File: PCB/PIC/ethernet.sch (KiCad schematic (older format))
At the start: 49 parts, among them J5 RJ45-TRANSFO, U1 LAN_8740, U2 SI502

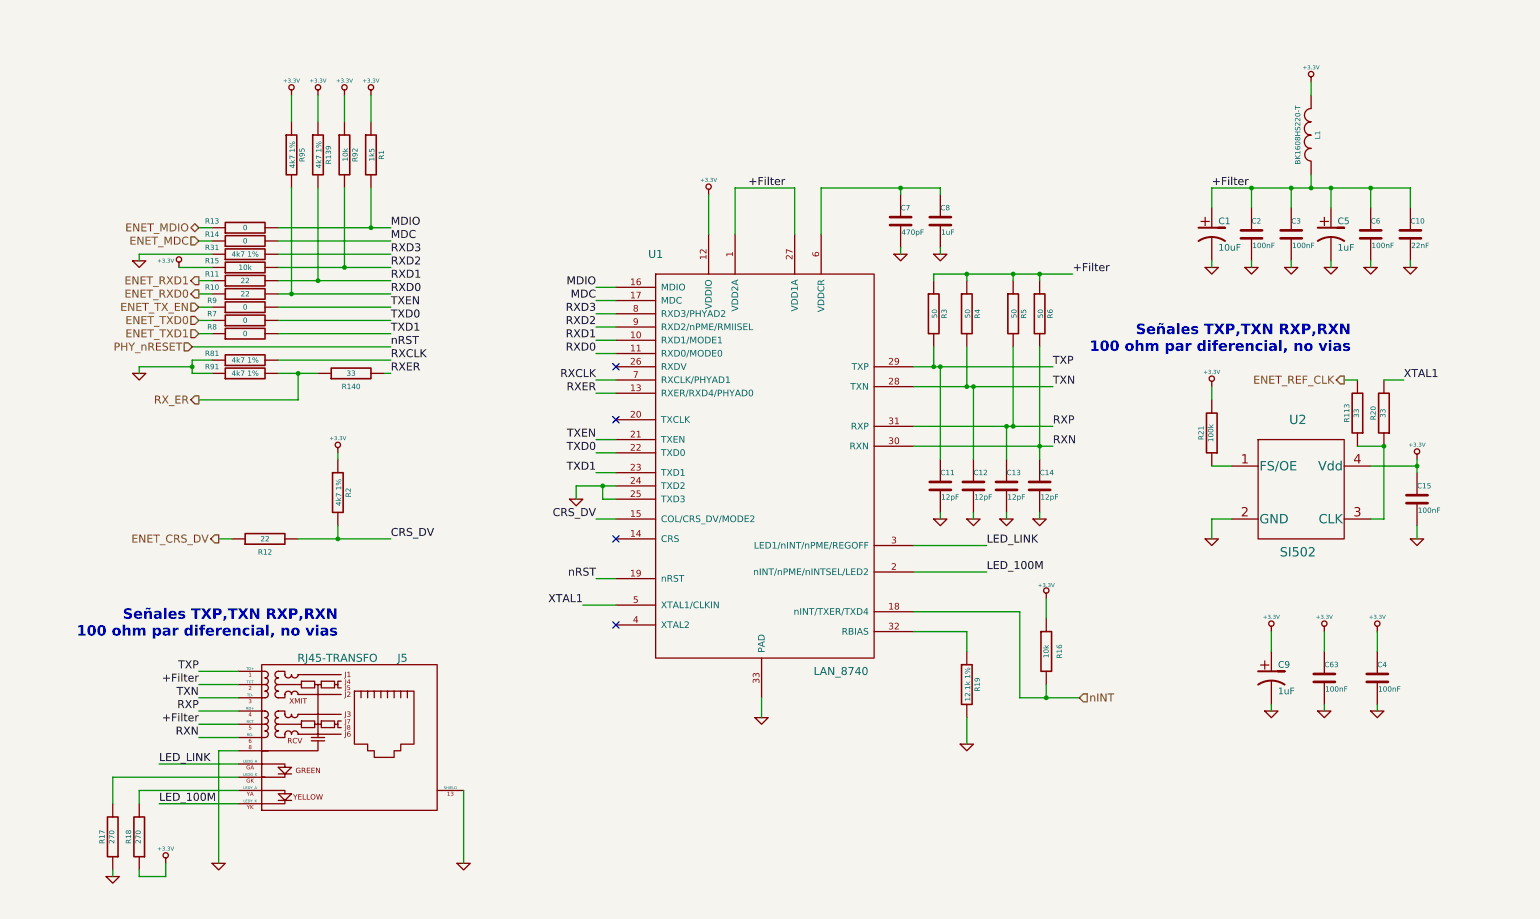
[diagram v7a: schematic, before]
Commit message: se completan pisadas componentes CIAA-PIC
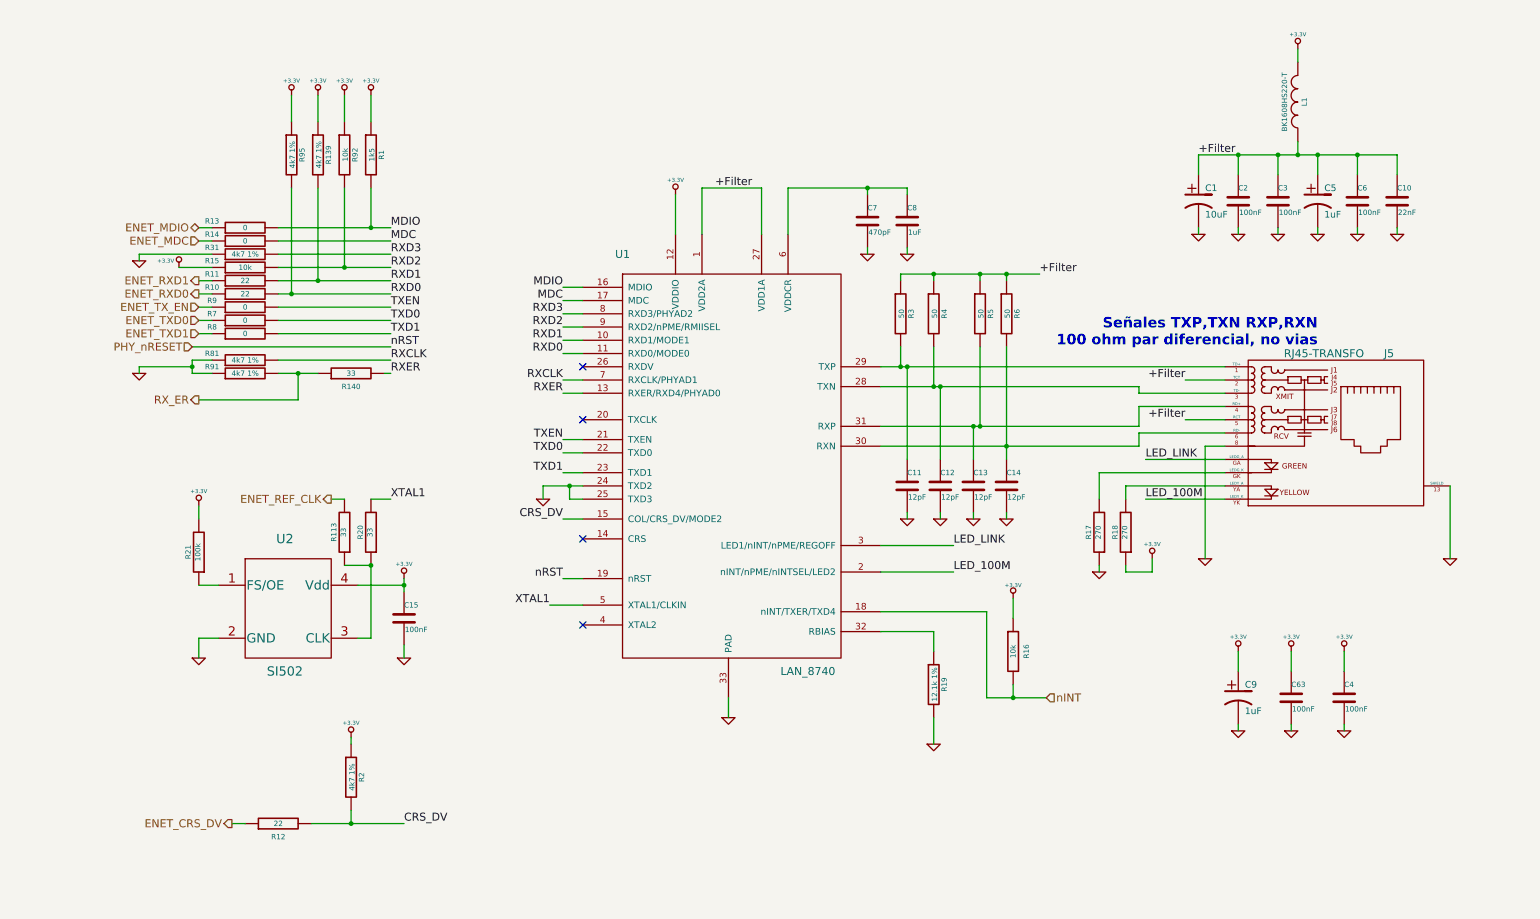
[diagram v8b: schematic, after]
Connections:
- net RXN: no longer names the net of C14.1, J5.6 (RD-), R6.2, U1.30 (RXN)
- net RXP: no longer names the net of C13.1, J5.4 (RD+), R5.2, U1.31 (RXP)
- net TXN: no longer names the net of C12.1, J5.3 (TD-), R4.2, U1.28 (TXN)
- net TXP: no longer names the net of C11.1, J5.1 (TD+), R3.2, U1.29 (TXP)
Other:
- moved on the sheet: C1, C10, C11, C12, C13, C14, C15, C2, C3, C4, C5, C6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
